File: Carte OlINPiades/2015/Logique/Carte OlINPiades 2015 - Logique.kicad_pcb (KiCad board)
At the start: 2 copper layers, 31 parts, among them U1 dsPIC33FJ128MC802, U2 LM7805, U3 LM2937-3.3

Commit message: enleve les anciennes pistes
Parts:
- moved C5 136.3 mm to (140.8, 177.3)
- moved C7 133.9 mm to (108.4, 135.6)
- moved U2 132.8 mm to (144.2, 163.6)
- moved U3 127.1 mm to (77.6, 113.4)
- moved C4 112.3 mm to (116.6, 171.4)
- moved Batteries1 111.0 mm to (136.2, 146.9)
- moved C6 105.9 mm to (89.2, 137.0)
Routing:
- net (no net): track 429.5 -> 0.00 mm
- net GND: track 452.9 -> 75.5 mm, vias 8 -> 0
- net +3.3V: track 250.9 -> 62.4 mm, vias 3 -> 0
- net +5V: track 155.1 -> 0.00 mm, vias 8 -> 0
- net RB11: track 149.7 -> 48.3 mm
- net RB10: track 142.7 -> 46.9 mm
- net RB7: track 163.2 -> 72.4 mm, vias 2 -> 0
- net RB6: track 144.9 -> 57.8 mm, vias 2 -> 0
- net RB9: track 139.4 -> 53.0 mm
- net RB8: track 138.8 -> 56.6 mm
- net RA2: track 117.1 -> 47.9 mm
- net RB3: track 136.3 -> 69.3 mm
- net RB2: track 111.7 -> 45.2 mm
- net Net-(DEMUX1-Pad16): track 130.4 -> 65.7 mm
- net Net-(DEMUX1-Pad15): track 123.4 -> 59.8 mm
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
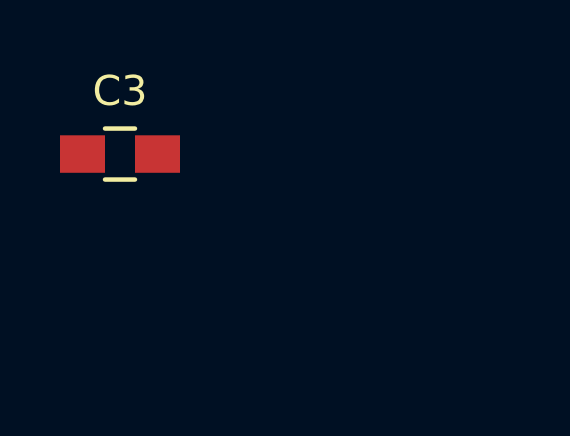
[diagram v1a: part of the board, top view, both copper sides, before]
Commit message: enleve condensateur inutile
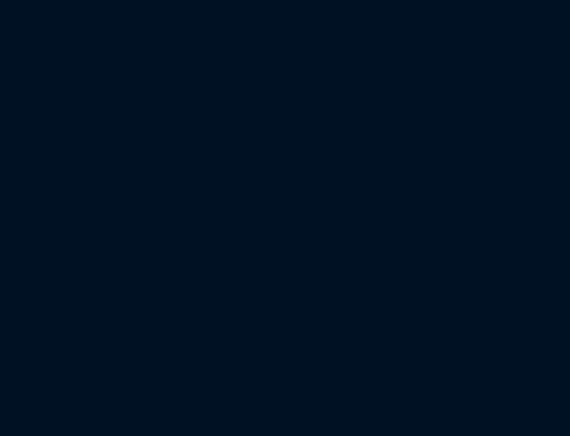
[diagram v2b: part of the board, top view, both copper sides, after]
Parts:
- removed C3: 15pF, Capacitors_SMD:C_0805_HandSoldering

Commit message: meilleur agencement
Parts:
- moved UART1 17.3 mm to (152.0, 75.5)
- moved UART2 17.3 mm to (152.0, 84.3)
- moved C2 7.84 mm to (123.2, 92.0)
- moved C9 6.00 mm to (134.0, 79.0), turned to 90 degrees
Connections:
- DEMUX1 pad 1: RB11 -> RB5
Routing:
- net RB5: track 0.00 -> 76.3 mm
- net RB11: track 48.3 -> 0.00 mm
- net RB3: track 69.3 -> 45.5 mm
- net GND: track 75.5 -> 58.8 mm
- net RB15: track 17.9 -> 32.9 mm
- net RB7: track 72.4 -> 57.8 mm
- net RB14: track 20.2 -> 33.9 mm
- net RB13: track 24.0 -> 33.3 mm
- net RB12: track 26.3 -> 34.7 mm
- net Net-(C2-Pad1): track 4.12 -> 11.4 mm
- net RB9: track 53.0 -> 53.7 mm
- net RB10: track 46.9 -> 46.2 mm
- net RB8: track 56.6 -> 57.1 mm

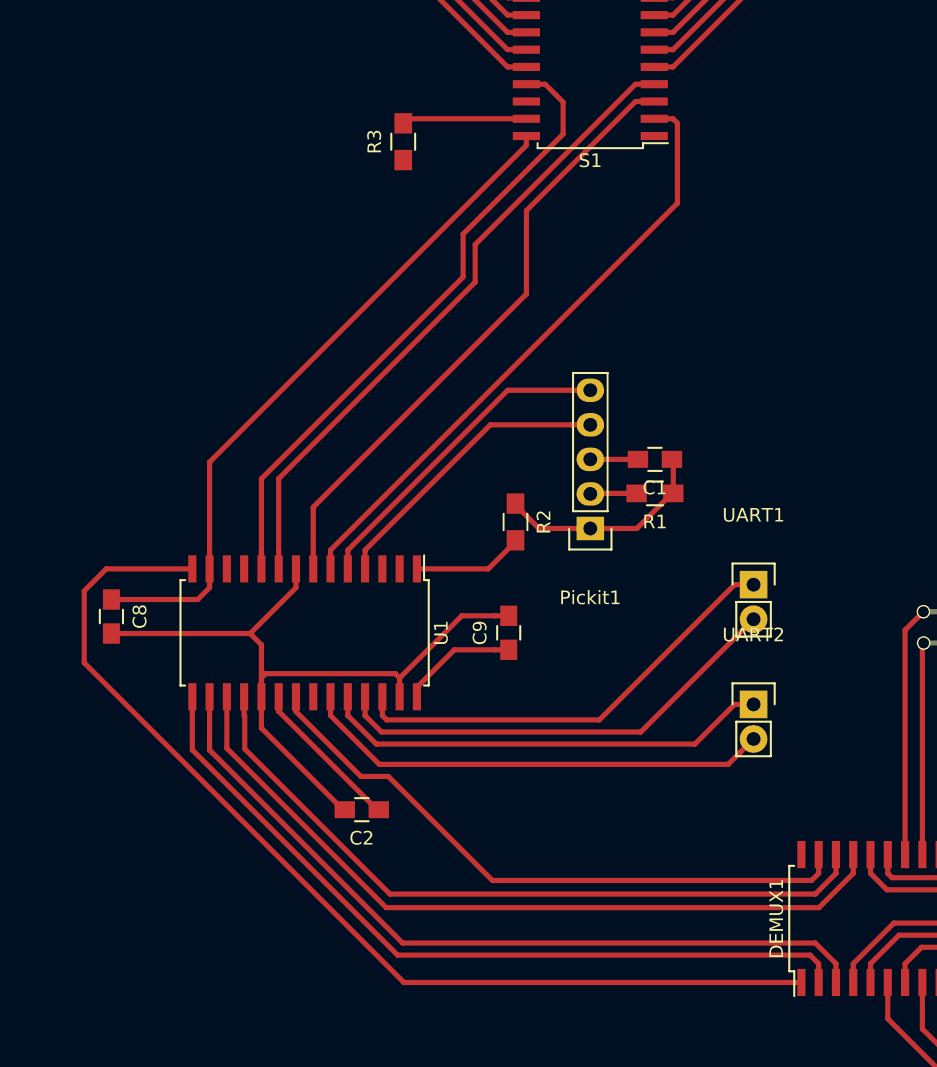
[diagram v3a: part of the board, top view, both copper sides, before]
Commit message: meilleur agencement coté driver
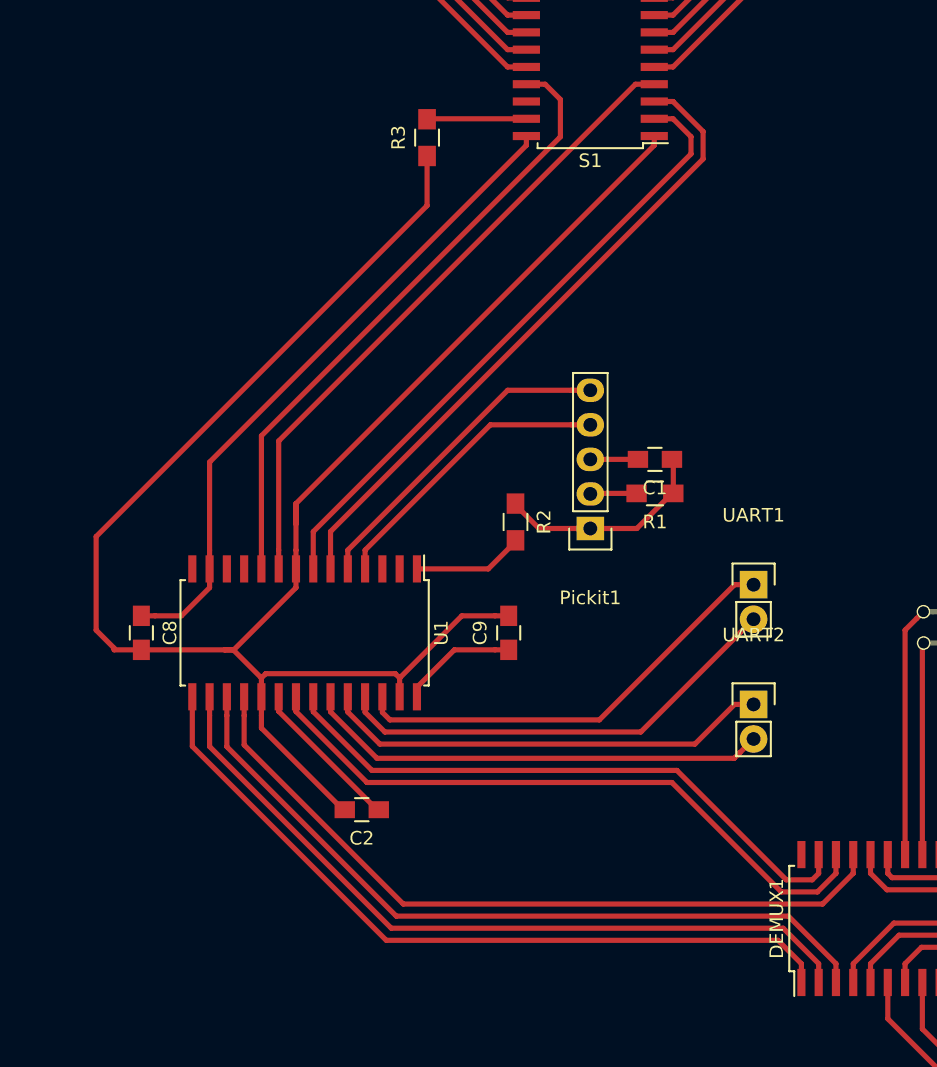
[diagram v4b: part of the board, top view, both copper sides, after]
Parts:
- moved C8 2.51 mm to (107.0, 79.0)
- moved R3 1.78 mm to (128.0, 42.6)
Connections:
- DEMUX1 pad 1: RB5 -> RB6
- DEMUX1 pad 2: RB6 -> RB7
- DEMUX1 pad 21: RB8 -> RB9
- DEMUX1 pad 22: RB9 -> RB10
- DEMUX1 pad 23: RB10 -> RB11
- DEMUX1 pad 3: RB7 -> RB8
- S1 pad 2: RB2 -> RB3
- S1 pad 3: RB3 -> RB2
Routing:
- net GND: track 58.8 -> 148.9 mm
- net RB5: track 76.3 -> 0.00 mm
- net RB11: track 0.00 -> 44.9 mm
- net RB2: track 45.2 -> 48.0 mm
- net RB10: track 46.2 -> 48.2 mm
- net Net-(R3-Pad2): track 9.19 -> 7.31 mm
- net RB9: track 53.7 -> 55.5 mm
- net +3.3V: track 62.4 -> 60.8 mm
- net RA3: track 48.1 -> 46.6 mm
- net RB6: track 57.8 -> 56.4 mm
- net RB7: track 57.8 -> 56.4 mm
- net RB3: track 45.5 -> 46.5 mm
- net RB8: track 57.1 -> 56.4 mm
- net RB12: track 34.7 -> 34.2 mm

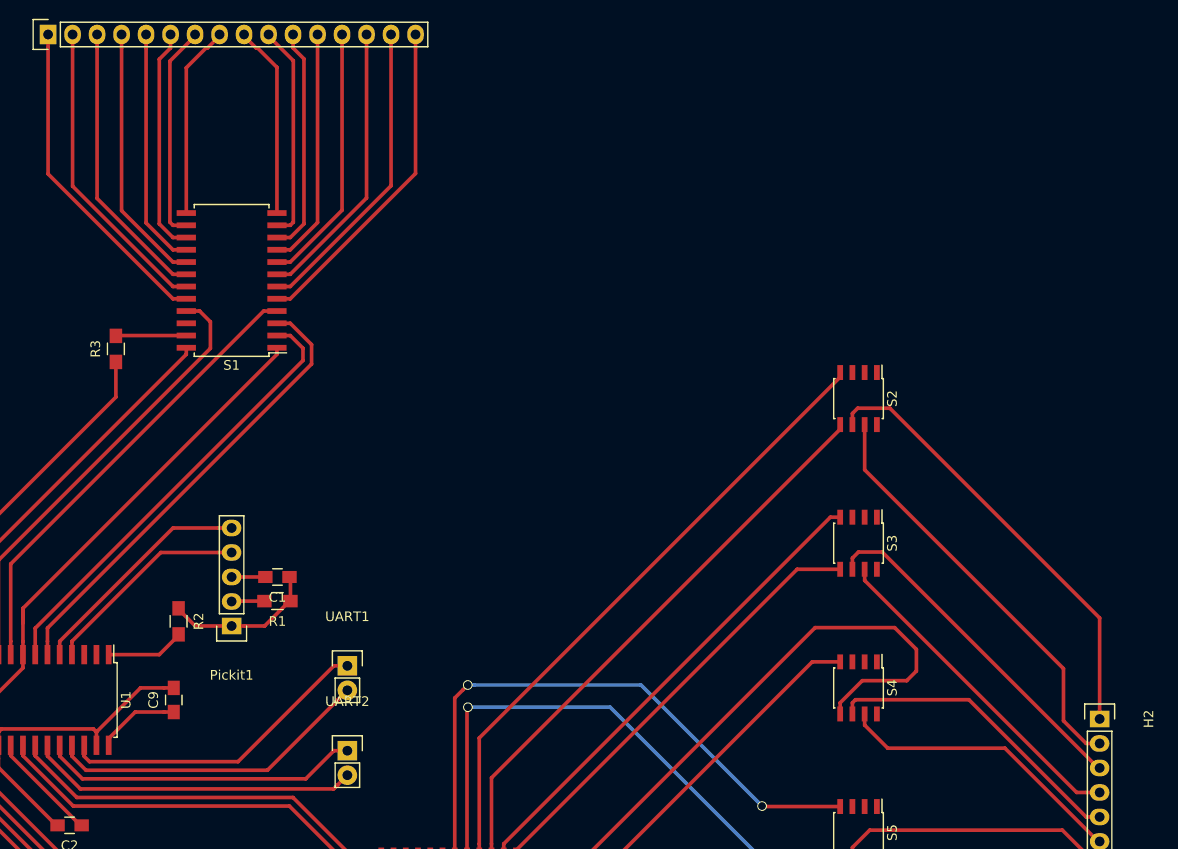
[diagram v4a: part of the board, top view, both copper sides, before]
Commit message: déplace les broche d'uart de de programmation
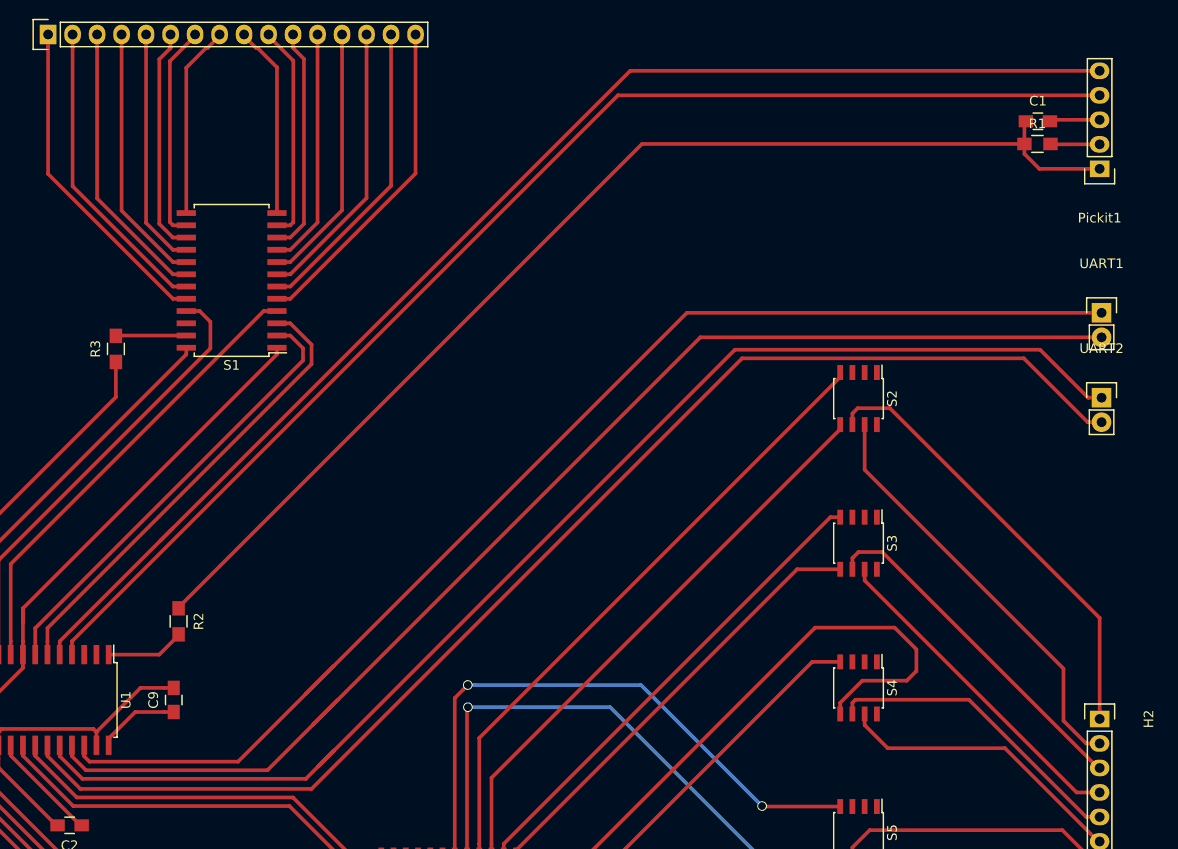
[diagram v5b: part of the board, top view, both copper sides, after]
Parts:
- moved Pickit1 101.7 mm to (230.0, 23.9)
- moved R1 92.0 mm to (223.6, 21.4), turned to 0 degrees
- moved C1 91.9 mm to (223.6, 19.0), turned to 0 degrees
- moved UART1 86.3 mm to (230.2, 38.9)
- moved UART2 86.3 mm to (230.2, 47.7)
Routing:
- net PGC: track 24.1 -> 135.5 mm
- net PGD: track 21.8 -> 131.4 mm
- net Net-(C1-Pad1): track 16.0 -> 119.7 mm
- net RB13: track 33.1 -> 132.9 mm
- net RB12: track 34.2 -> 133.1 mm
- net RB15: track 32.8 -> 130.3 mm
- net RB14: track 33.7 -> 130.6 mm
- net +3.3V: track 60.8 -> 62.6 mm
- net GND: track 148.9 -> 150.6 mm

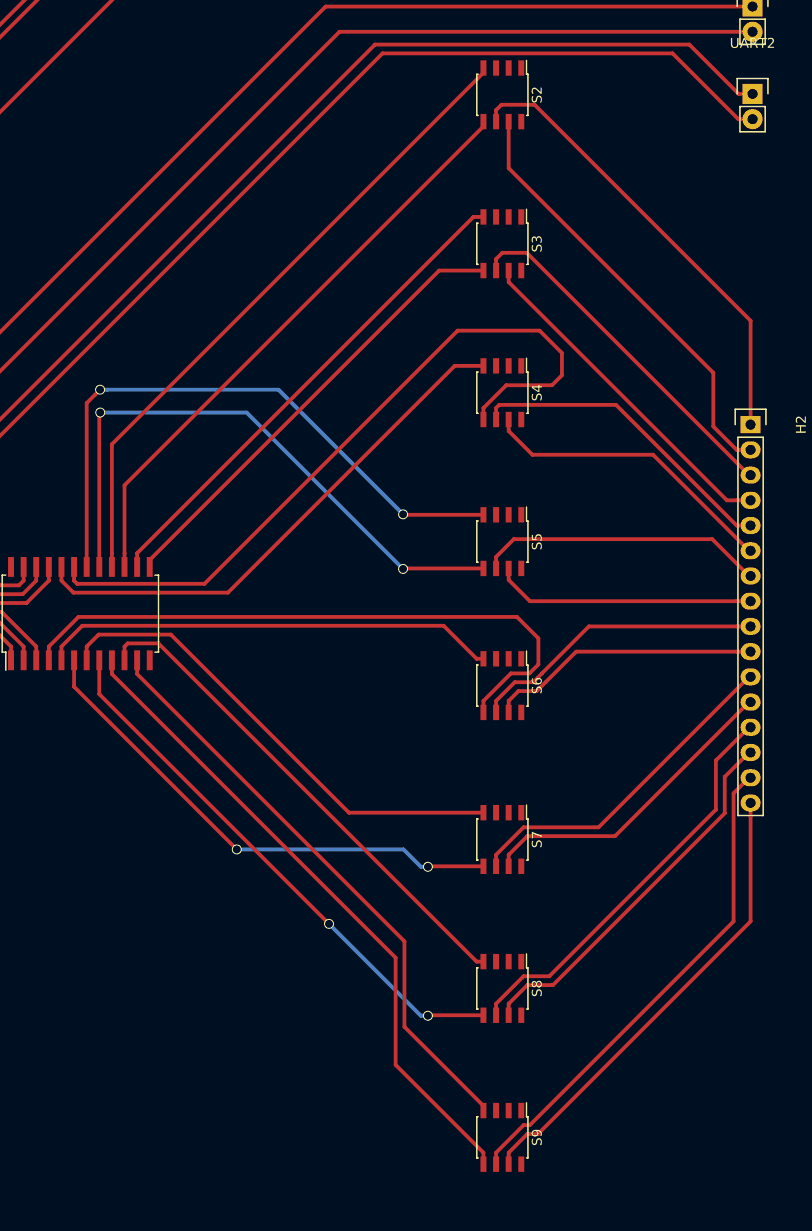
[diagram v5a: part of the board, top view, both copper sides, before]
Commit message: resserre les switchs
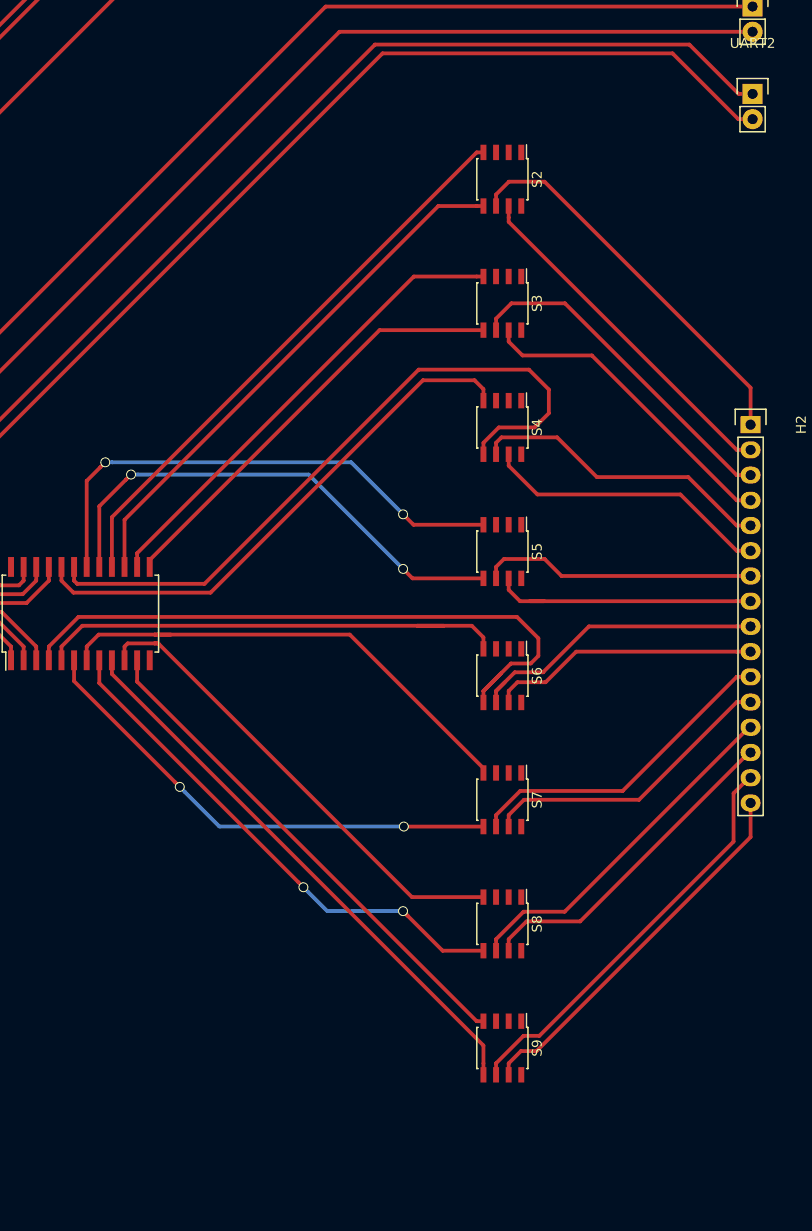
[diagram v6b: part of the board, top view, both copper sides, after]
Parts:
- moved S9 9.00 mm to (205.0, 143.8)
- moved S2 8.50 mm to (205.0, 56.2)
- moved S8 6.50 mm to (205.0, 131.2)
- moved S3 6.00 mm to (205.0, 68.8)
- moved S7 4.00 mm to (205.0, 118.8)
- moved S4 3.50 mm to (205.0, 81.2)
- moved S5 1.00 mm to (205.0, 93.8)
- moved S6 1.00 mm to (205.0, 106.2)
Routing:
- net Net-(DEMUX1-Pad17): track 60.7 -> 50.5 mm
- net Net-(DEMUX1-Pad18): track 62.2 -> 52.1 mm
- net Net-(DEMUX1-Pad9): track 66.2 -> 57.2 mm
- net Net-(H2-Pad16): track 47.1 -> 38.4 mm
- net Net-(DEMUX1-Pad11): track 59.8 -> 51.2 mm
- net Net-(H2-Pad2): track 44.0 -> 35.5 mm
- net Net-(H2-Pad15): track 50.0 -> 41.6 mm
- net Net-(DEMUX1-Pad16): track 65.7 -> 57.6 mm
- net Net-(H2-Pad1): track 46.5 -> 39.6 mm
- net Net-(DEMUX1-Pad15): track 59.8 -> 54.0 mm
- net Net-(H2-Pad13): track 41.2 -> 35.6 mm
- net Net-(H2-Pad14): track 38.2 -> 33.3 mm
- net Net-(DEMUX1-Pad19): track 74.8 -> 70.5 mm
- net Net-(DEMUX1-Pad5): track 46.1 -> 49.0 mm
- net Net-(DEMUX1-Pad8): track 55.5 -> 52.9 mm
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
